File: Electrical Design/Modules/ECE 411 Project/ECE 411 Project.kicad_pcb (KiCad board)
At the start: 2 copper layers, 99.2 x 99.2 mm, 129 parts, among them J1 5mm 9V Barrel, J2 BOOST, J3 Pheonix Connector, J4 1/8in Jack, J5 1/4in Jack, Q2 2N3904, Q3 2N3904, Q4 2N3904, Q5 PNP, Q6 PNP, SW1 SW_Push, SW2 SW_Push, SW3 SW_Push, SW4 SW_Push, SW5 SW_Push, SW6 SW_Push, SW7 SW_Push, SW8 SW_Push, SW9 SW_SPDT, U1 HT7333, U2 LT1054, U3 MN3207, U4 NE555D, U5 LTV-827, U9 TPA3136D2PWPR

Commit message: schematic update
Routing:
- net /ESP32-S3-WROOM Dev Board/GENOUT: track 83.6 -> 116.2 mm, vias 2 -> 3
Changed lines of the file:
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@@
+	)
+	(segment
+		(start 77.9625 35.909448)
+		(end 77.9625 36.7125)
+		(width 0.4)
+		(layer "F.Cu")
+		(net 38)
 	)
 	(segment
@@
 		(net 38)
 	)
+	(segment
+		(start 77.9625 36.7125)
+		(end 79 37.75)
+		(width 0.4)
+		(layer "F.Cu")
+		(net 38)
+	)
 	(via
 		(at 59.8 36.3)
+		(size 0.6)
+		(drill 0.3)
+		(layers "F.Cu" "B.Cu")
+		(free yes)
+		(net 38)
+	)
+	(via
+		(at 79 37.75)
 		(size 0.6)
 		(drill 0.3)
@@
 	)
 	(segment
+		(start 86.45 30.3)
+		(end 98.22 30.3)
+		(width 0.4)
+		(layer "B.Cu")
+		(net 38)
+	)
+	(segment
+		(start 79 37.75)
+		(end 86.45 30.3)
+		(width 0.4)
+		(layer "B.Cu")
+		(net 38)
+	)
+	(segment
 		(start 41.3 41.9)
 		(end 54.2 41.9)
@@
 		(layer "B.Cu")
 		(net 38)
+	)
+	(segment
+		(start 98.22 30.3)
+		(end 103.92 36)
+		(width 0.4)
+		(layer "B.Cu")
+		(net 38)

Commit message: pcb amp revision
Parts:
- removed C2: 4.7uF, Capacitor_SMD:C_1206_3216Metric_Pad1.33x1.80mm_HandSolder
- removed C20: 6.8nF, Capacitor_SMD:C_0805_2012Metric_Pad1.18x1.45mm_HandSolder
- removed C21, C23: 1uF, Capacitor_SMD:C_0805_2012Metric_Pad1.18x1.45mm_HandSolder
- removed CHO-TRE1, OUT_{LINE}1: TestPoint, TestPoint:TestPoint_THTPad_2.5x2.5mm_Drill1.2mm
- removed D3: LED, LED_THT:LED_D5.0mm
- removed R1, R2: 1.2k, Resistor_SMD:R_0805_2012Metric_Pad1.20x1.40mm_HandSolder
- removed R34: 47k, Resistor_SMD:R_0805_2012Metric_Pad1.20x1.40mm_HandSolder
- removed R35: 10k, Resistor_SMD:R_0805_2012Metric_Pad1.20x1.40mm_HandSolder
- removed R36: 470, Resistor_SMD:R_0805_2012Metric_Pad1.20x1.40mm_HandSolder
- removed R37: 100k, Resistor_SMD:R_0805_2012Metric_Pad1.20x1.40mm_HandSolder
- removed R39: 1k, Resistor_SMD:R_0805_2012Metric_Pad1.20x1.40mm_HandSolder
- removed RV1, RV2, RV3, RV7: 10k, Connector_PinSocket_2.54mm:PinSocket_1x03_P2.54mm_Vertical
- removed RV4: 100k Pot, Connector_PinHeader_2.54mm:PinHeader_1x03_P2.54mm_Vertical
- removed RV5: 1k, Connector_PinHeader_2.54mm:PinHeader_1x03_P2.54mm_Vertical
- removed RV6: 100k, Connector_PinSocket_2.54mm:PinSocket_1x03_P2.54mm_Vertical
- removed U4: NE555D, Package_SO:SOIC-8_3.9x4.9mm_P1.27mm
- removed U5: LTV-827, Package_DIP:DIP-8_W7.62mm
- removed V3207D2: ~, Package_DIP:CERDIP-8_W7.62mm_SideBrazed
- added G***: LOGO, LOGO, F.Cu at (103.1, 117.1)
- added M4: MountingHole_4.3mm_M4_Pad_TopBottom, MountingHole:MountingHole_4.3mm_M4_Pad_TopBottom, F.Cu at (38.4, 117.5)
- added REF**: MountingHole_4.3mm_M4_Pad_TopBottom, MountingHole:MountingHole_4.3mm_M4_Pad_TopBottom, F.Cu at (125.1, 118.6)
- C33: value .1uF -> 0.1uF
- J5: value 1/4in Jack -> 01x02 pin header
- L1, L2: footprint Inductor-VLS6045AF_330M:IND_VLS6045AF-330M -> Inductor_THT:RL110-330K-RC
- moved GND1 91.6 mm to (125.1, 96.6)
- moved C28 17.3 mm to (69.0, 101.0)
- moved R40 14.1 mm to (79.0, 109.0), turned to -90 degrees
- moved C29 13.7 mm to (72.2, 95.2), turned to -90 degrees
- moved J5 12.2 mm to (77.9, 97.7), turned to 90 degrees
- moved ? 11.9 mm to (117.8, 113.8)
- moved C26 10.9 mm to (69.7, 95.2), turned to -90 degrees
- moved C24 9.73 mm to (65.9, 96.7), turned to 180 degrees
- moved C37 8.76 mm to (54.0, 96.2)
- moved C33 8.76 mm to (80.0, 103.8), turned to 0 degrees
- moved C32 8.30 mm to (80.0, 106.0)
- moved C27 8.03 mm to (72.0, 116.1)
- moved R43 7.88 mm to (76.0, 101.0)
- moved C35 7.81 mm to (64.9, 104.7), turned to 0 degrees
- moved U9 7.75 mm to (72.2, 107.6)
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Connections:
- SW8 pad 2: /ESP32-S3-WROOM Dev Board/BTN7 -> /BTN7
- U6 pad 13: /ESP32-S3-WROOM Dev Board/SCL -> unconnected-(U6-IO12-Pad13)
- U6 pad 15: /ESP32-S3-WROOM Dev Board/SDA -> GND
- U6 pad 23: /ESP32-S3-WROOM Dev Board/BTN7 -> unconnected-(U6-IO15-Pad23)
- U6 pad 24: /ESP32-S3-WROOM Dev Board/CLK -> unconnected-(U6-IO2-Pad24)
- U6 pad 25: unconnected-(U6-IO0-Pad25) -> /ESP32-S3-WROOM Dev Board/BTN6
- U6 pad 26: unconnected-(U6-IO4-Pad26) -> /ESP32-S3-WROOM Dev Board/BTN5
- U6 pad 27: /ESP32-S3-WROOM Dev Board/BTN6 -> /ESP32-S3-WROOM Dev Board/BTN4
- U6 pad 28: /ESP32-S3-WROOM Dev Board/BTN5 -> /ESP32-S3-WROOM Dev Board/BTN3
- U6 pad 29: /ESP32-S3-WROOM Dev Board/BTN4 -> /ESP32-S3-WROOM Dev Board/BTN2
- U6 pad 30: /ESP32-S3-WROOM Dev Board/BTN3 -> /ESP32-S3-WROOM Dev Board/BTN1
- U6 pad 31: /ESP32-S3-WROOM Dev Board/BTN2 -> /ESP32-S3-WROOM Dev Board/BTN0
- U6 pad 33: /ESP32-S3-WROOM Dev Board/BTN1 -> /ESP32-S3-WROOM Dev Board/SDA
- U6 pad 35: /ESP32-S3-WROOM Dev Board/BTN0 -> unconnected-(U6-TXD0/IO1-Pad35)
- U6 pad 36: unconnected-(U6-IO22-Pad36) -> /ESP32-S3-WROOM Dev Board/SCL
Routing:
- net /Tremolo Effect/TREMOUT: track 102.9 -> 0.00 mm, vias 1 -> 0
- net +9V: track 232.4 -> 162.8 mm
- net /Chorus Effect/CHORUSIN: track 80.7 -> 19.2 mm
- net /Chorus Effect/CHORUSOUT: track 51.5 -> 0.00 mm, vias 2 -> 0
- net Net-(V3207D2-+): track 59.3 -> 16.2 mm, vias 2 -> 0
- net Vin: track 130.9 -> 171.0 mm, vias 8 -> 4
- net /ESP32-S3-WROOM Dev Board/BTN7: track 36.5 -> 0.00 mm
- net (no net): track 0.00 -> 36.5 mm
- net /ESP32-S3-WROOM Dev Board/GENOUT: track 116.2 -> 85.8 mm
- net Net-(U4-THR): track 21.7 -> 0.00 mm, vias 2 -> 0
- net /LineOut: track 17.8 -> 4.15 mm
- net Net-(U4-DIS): track 12.4 -> 0.00 mm
- net +4.5V: track 104.1 -> 92.2 mm
- net /Class-D Amplification/SPK+: track 30.5 -> 42.1 mm
- net Net-(Q6-E): track 22.8 -> 11.9 mm
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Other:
- board size 99.2 x 99.2 mm -> 99.2 x 97.1 mm
- board text added: "1/4{dblquote} OUT"
- board text added: "LINE OUT"

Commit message: pcb redo b2.1
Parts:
- removed CLK1: TestPoint, TestPoint:TestPoint_THTPad_2.5x2.5mm_Drill1.2mm
- removed SW8: SW_Push, Connector_PinHeader_2.54mm:PinHeader_1x02_P2.54mm_Vertical
- added C2: 4.7uF, Capacitor_SMD:C_1206_3216Metric_Pad1.33x1.80mm_HandSolder, F.Cu at (151.5, 126.8)
- added C20: 6.8nF, Capacitor_SMD:C_0805_2012Metric_Pad1.18x1.45mm_HandSolder, F.Cu at (190.1, 89.8)
- added C21: 1uF, Capacitor_SMD:C_0805_2012Metric_Pad1.18x1.45mm_HandSolder, F.Cu at (190.1, 92.8)
- added C23: 1uF, Capacitor_SMD:C_0805_2012Metric_Pad1.18x1.45mm_HandSolder, F.Cu at (161.5, 106.3)
- added CHO-TRE1: TestPoint, TestPoint:TestPoint_THTPad_2.5x2.5mm_Drill1.2mm, F.Cu at (110.7, 37.0)
- added D3: LED, LED_THT:LED_D5.0mm, F.Cu at (151.0, 121.4)
- added J6: 1x2header, Connector_PinSocket_2.54mm:PinSocket_1x02_P2.54mm_Vertical, F.Cu at (139.0, 100.0)
- added J7: 1x2header, Connector_PinSocket_2.54mm:PinSocket_1x02_P2.54mm_Vertical, F.Cu at (92.8, 42.3)
- added OUT_{LINE}1: TestPoint, TestPoint:TestPoint_THTPad_2.5x2.5mm_Drill1.2mm, F.Cu at (151.4, 111.7)
- added R1: 1.2k, Resistor_SMD:R_0805_2012Metric_Pad1.20x1.40mm_HandSolder, F.Cu at (153.1, 130.8)
- added R2: 1.2k, Resistor_SMD:R_0805_2012Metric_Pad1.20x1.40mm_HandSolder, F.Cu at (153.1, 133.8)
- added R34: 47k, Resistor_SMD:R_0805_2012Metric_Pad1.20x1.40mm_HandSolder, F.Cu at (190.1, 78.0)
- added R35: 10k, Resistor_SMD:R_0805_2012Metric_Pad1.20x1.40mm_HandSolder, F.Cu at (190.1, 80.9)
- added R36: 470, Resistor_SMD:R_0805_2012Metric_Pad1.20x1.40mm_HandSolder, F.Cu at (190.1, 83.8)
- added R37: 100k, Resistor_SMD:R_0805_2012Metric_Pad1.20x1.40mm_HandSolder, F.Cu at (190.1, 86.8)
- added R39: 1k, Resistor_SMD:R_0805_2012Metric_Pad1.20x1.40mm_HandSolder, F.Cu at (156.1, 109.8)
- added R9: 4.7k, Resistor_SMD:R_0805_2012Metric_Pad1.20x1.40mm_HandSolder, F.Cu at (78.9, 32.7)
- added REF**: MountingHole_4.3mm_M4_Pad_TopBottom, MountingHole:MountingHole_4.3mm_M4_Pad_TopBottom, F.Cu at (126.6, 28.7)
- added REF**: MountingHole_4.3mm_M4_Pad_TopBottom, MountingHole:MountingHole_4.3mm_M4_Pad_TopBottom, F.Cu at (36.7, 28.7)
- added RV1: 10k, Connector_PinSocket_2.54mm:PinSocket_1x02_P2.54mm_Vertical, F.Cu at (94.9, 29.4)
- added RV2: 10k, Connector_PinSocket_2.54mm:PinSocket_1x02_P2.54mm_Vertical, F.Cu at (110.7, 29.3)
- added RV3: 10k, Connector_PinSocket_2.54mm:PinSocket_1x02_P2.54mm_Vertical, F.Cu at (157.4, 100.0)
- added RV4: 100k Pot, Connector_PinHeader_2.54mm:PinHeader_1x03_P2.54mm_Vertical, F.Cu at (90.8, 29.3)
- added RV5: 1k, Connector_PinSocket_2.54mm:PinSocket_1x03_P2.54mm_Vertical, F.Cu at (86.5, 29.3)
- added RV6: 100k, Connector_PinSocket_2.54mm:PinSocket_1x02_P2.54mm_Vertical, F.Cu at (140.0, 131.7)
- added RV7: 10k, Connector_PinSocket_2.54mm:PinSocket_1x02_P2.54mm_Vertical, F.Cu at (80.3, 92.2)
- added RV8: 100k, Connector_PinSocket_2.54mm:PinSocket_1x03_P2.54mm_Vertical, F.Cu at (77.3, 29.2)
- added SW10: SW_SPDT, Button_Switch_THT:SW_Slide_SPDT_Angled_CK_OS102011MA1Q, F.Cu at (104.8, 26.9)
- added TP1: Line In, TestPoint:TestPoint_Bridge_Pitch2.0mm_Drill0.7mm, F.Cu at (155.4, 106.5)
- added U4: NE555D, Package_SO:SOIC-8_3.9x4.9mm_P1.27mm, F.Cu at (146.5, 132.7)
- added U5: LTV-827, Package_DIP:DIP-8_W7.62mm, F.Cu at (139.3, 119.7)
- added V3207D2: ~, Package_DIP:CERDIP-8_W7.62mm_SideBrazed, F.Cu at (178.5, 80.0)
- J5: value 01x02 pin header -> 1x2 header
- moved V4.5 96.6 mm to (149.4, 142.3)
- moved C18 80.5 mm to (173.1, 67.2)
- moved C19 80.5 mm to (173.1, 70.2), turned to 0 degrees
- moved C17 74.3 mm to (173.1, 64.1)
- moved R32 63.8 mm to (152.2, 81.8), turned to 0 degrees
- moved C15 61.9 mm to (168.3, 70.2), turned to 0 degrees
- moved C16 60.1 mm to (168.3, 73.2)
- moved U3 59.3 mm to (156.2, 83.6), turned to 0 degrees
- moved Q4 58.5 mm to (156.6, 77.5), turned to 0 degrees
- moved C41 55.8 mm to (173.1, 73.2), turned to 0 degrees
- moved R3 53.6 mm to (142.7, 64.1), turned to 0 degrees
- moved C13 53.1 mm to (168.3, 64.1), turned to 0 degrees
- moved C14 48.9 mm to (168.3, 67.2)
- moved Q3 48.2 mm to (156.6, 71.7), turned to 0 degrees
- moved R31 48.1 mm to (152.2, 78.9), turned to 0 degrees
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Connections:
- net /ESP32-S3-WROOM Dev Board/SCL renamed /SCL
- net /ESP32-S3-WROOM Dev Board/SDA renamed /SDA
- C38 pad 1: /ESP32-S3-WROOM Dev Board/GENOUT -> /FX
- FUZ-CHO1 pad 1: /Chorus Effect/CHORUSIN -> /Fuzz Schematic/FUZZOUT
- Q2 pad 3: +9V -> /Chorus Effect/Vin
- Q3 pad 3: +9V -> /Chorus Effect/Vin
- Q4 pad 3: +9V -> /Chorus Effect/Vin
- R16 pad 2: +4.5V -> /Chorus Effect/V.5in
- R20 pad 1: +4.5V -> /Chorus Effect/V.5in
- R28 pad 2: +4.5V -> /Chorus Effect/V.5in
- SW3 pad 2: /ESP32-S3-WROOM Dev Board/BTN2 -> /ESP32-S3-WROOM Dev Board/BTN1
- SW9 pad 1: /ESP32-S3-WROOM Dev Board/GENOUT -> /FX
- SW9 pad 3: /Tremolo Effect/TREMOUT -> /Amp
- U6 pad 1: unconnected-(U6-3V3-Pad1) -> /ESP32-S3-WROOM Dev Board/MCU3v3
- U6 pad 10: unconnected-(U6-IO26-Pad10) -> /ESP32-S3-WROOM Dev Board/BTN3
- U6 pad 11: unconnected-(U6-IO27-Pad11) -> /ESP32-S3-WROOM Dev Board/BTN1
- U6 pad 12: unconnected-(U6-IO14-Pad12) -> /ESP32-S3-WROOM Dev Board/BTN1
- U6 pad 13: unconnected-(U6-IO12-Pad13) -> /ESP32-S3-WROOM Dev Board/BTN0
- U6 pad 25: /ESP32-S3-WROOM Dev Board/BTN6 -> unconnected-(U6-IO0-Pad25)
- U6 pad 26: /ESP32-S3-WROOM Dev Board/BTN5 -> unconnected-(U6-IO4-Pad26)
- U6 pad 27: /ESP32-S3-WROOM Dev Board/BTN4 -> unconnected-(U6-IO16-Pad27)
- U6 pad 28: /ESP32-S3-WROOM Dev Board/BTN3 -> unconnected-(U6-IO17-Pad28)
- U6 pad 29: /ESP32-S3-WROOM Dev Board/BTN2 -> unconnected-(U6-IO5-Pad29)
- U6 pad 30: /ESP32-S3-WROOM Dev Board/BTN1 -> unconnected-(U6-IO18-Pad30)
- U6 pad 31: /ESP32-S3-WROOM Dev Board/BTN0 -> unconnected-(U6-IO19-Pad31)
- U6 pad 5: unconnected-(U6-IO34-Pad5) -> /ESP32-S3-WROOM Dev Board/FREQ
- U6 pad 6: unconnected-(U6-IO35-Pad6) -> /FX
- U6 pad 7: unconnected-(U6-IO32-Pad7) -> /ESP32-S3-WROOM Dev Board/BTN6
- U6 pad 8: unconnected-(U6-IO33-Pad8) -> /ESP32-S3-WROOM Dev Board/BTN5
- U6 pad 9: /ESP32-S3-WROOM Dev Board/GENOUT -> /ESP32-S3-WROOM Dev Board/BTN4
- V3207D1 pad 3: +9V -> /Chorus Effect/Vin
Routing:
- net /FX: track 0.00 -> 94.5 mm
- net +4.5V: track 92.2 -> 2.00 mm, vias 6 -> 0
- net /ESP32-S3-WROOM Dev Board/GENOUT: track 85.8 -> 0.00 mm, vias 3 -> 0
- net Net-(U3-IN): track 53.0 -> 0.00 mm
- net +9V: track 162.8 -> 111.6 mm, vias 5 -> 3
- net /SDA: track 54.8 -> 5.15 mm
- net /Amp: track 0.00 -> 47.3 mm, vias 0 -> 2
- net /SCL: track 52.3 -> 5.25 mm
- net (no net): track 36.5 -> 0.00 mm
- net Net-(C12-Pad1): track 34.8 -> 0.00 mm
- net Net-(Q6-E): track 11.9 -> 36.8 mm
- net Net-(U3-OUT1): track 22.2 -> 0.00 mm
- net Net-(Q4-E): track 20.8 -> 0.00 mm
- net /Fuzz Schematic/FUZZOUT: track 0.00 -> 19.6 mm
- net +5V: track 118.3 -> 99.6 mm
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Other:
- board size 99.2 x 97.1 mm -> 99.8 x 99.9 mm
- board text added: "Vol"
- board text added: "r1.4 | 17 November 2024"
- board text removed: "r1.1 14 November 2024"

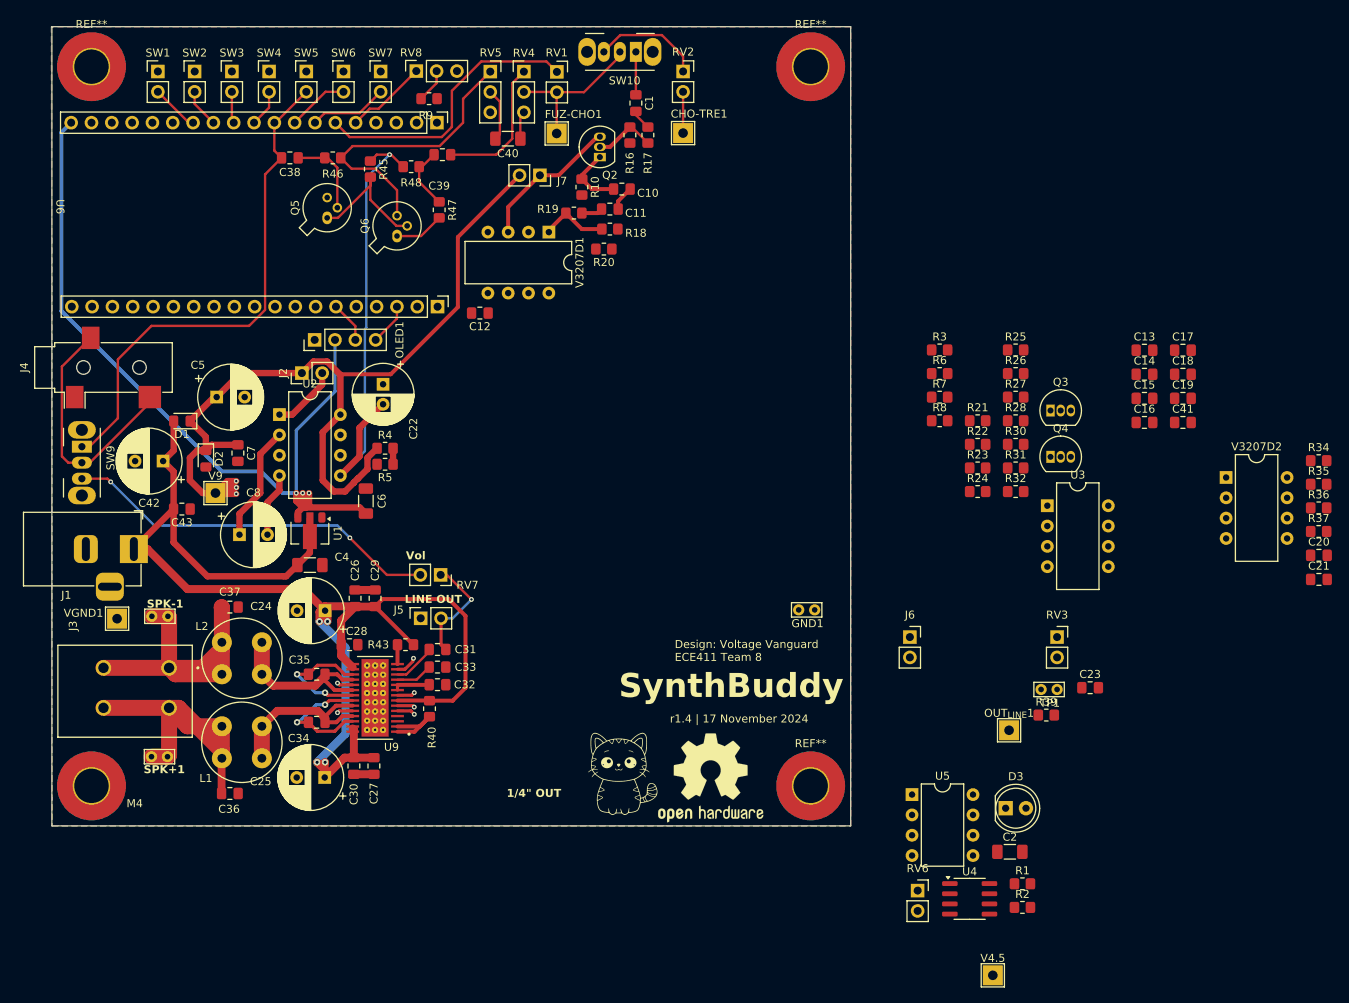
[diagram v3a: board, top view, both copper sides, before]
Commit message: new space-optimized PCB layout
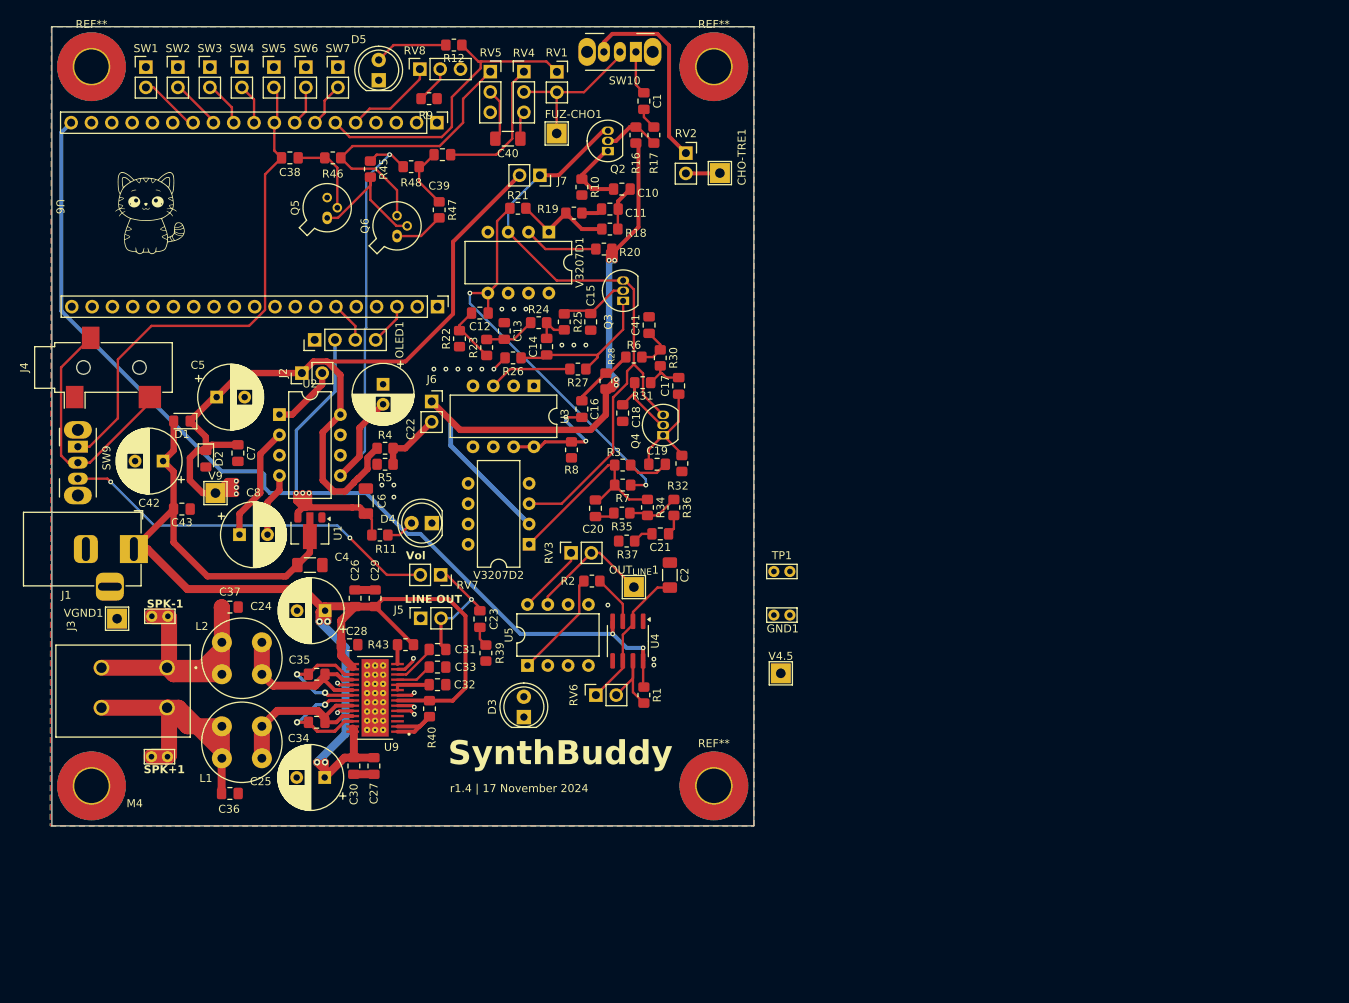
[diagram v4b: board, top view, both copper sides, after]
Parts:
- removed ?: , clipboard:cb89ceac-0acd-432b-9393-97274f22b4f5
- added D4: LED, LED_THT:LED_D5.0mm, F.Cu at (79.2, 85.8)
- added D5: LED, LED_THT:LED_D5.0mm, F.Cu at (72.6, 30.4)
- added R11: 1.2k, Resistor_SMD:R_0805_2012Metric_Pad1.20x1.40mm_HandSolder, F.Cu at (72.8, 87.2)
- added R12: 1.2k, Resistor_SMD:R_0805_2012Metric_Pad1.20x1.40mm_HandSolder, F.Cu at (82.0, 26.0)
- moved G*** 91.7 mm to (44.0, 47.0)
- moved C20 90.6 mm to (99.7, 83.9), turned to -90 degrees
- moved V3207D2 87.5 mm to (91.4, 88.4), turned to 180 degrees
- moved R35 87.2 mm to (103.0, 84.5)
- moved R37 86.5 mm to (103.6, 88.0)
- moved R34 84.1 mm to (106.2, 83.8), turned to -90 degrees
- moved C21 82.5 mm to (107.8, 87.1), turned to 180 degrees
- moved R36 80.6 mm to (109.5, 83.8), turned to -90 degrees
- moved C13 80.1 mm to (88.3, 61.7), turned to -90 degrees
- moved C23 76.8 mm to (85.2, 97.8), turned to -90 degrees
- moved C14 74.8 mm to (93.6, 63.7), turned to 90 degrees
- moved R39 70.5 mm to (86.0, 102.0), turned to 90 degrees
- moved C16 70.3 mm to (98.0, 71.5), turned to 90 degrees
- moved C18 70.2 mm to (103.1, 72.0), turned to 90 degrees
- moved C15 69.9 mm to (99.1, 60.6), turned to 90 degrees
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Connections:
- R1 pad 1: +9V -> +5V
- U4 pad 4: +9V -> +5V
- U4 pad 8: +9V -> +5V
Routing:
- net /Chorus Effect/V.5in: track 0.00 -> 85.8 mm, vias 0 -> 4
- net /Chorus Effect/Vin: track 18.2 -> 80.7 mm
- net +5V: track 99.6 -> 161.6 mm, vias 3 -> 5
- net Net-(C12-Pad1): track 0.00 -> 51.5 mm, vias 0 -> 2
- net Net-(V3207D2-+): track 0.00 -> 25.3 mm
- net Net-(Q3-E): track 0.00 -> 20.2 mm
- net Net-(U4-THR): track 0.00 -> 18.2 mm
- net /Amp: track 47.3 -> 63.6 mm
- net Net-(U3-OUT1): track 0.00 -> 15.4 mm, vias 0 -> 2
- net Net-(Q4-E): track 0.00 -> 13.9 mm
- net Net-(R2-Pad2): track 0.00 -> 13.5 mm
- net Net-(U4-DIS): track 0.00 -> 11.0 mm
- net Net-(SW10-C): track 13.8 -> 24.7 mm
- net Net-(U3-IN): track 0.00 -> 10.4 mm
- net /Chorus Effect/CHORUSOUT: track 5.16 -> 15.5 mm
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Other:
- board size 99.8 x 99.9 mm -> 87.8 x 99.9 mm
- board text removed: "1/4{dblquote} OUT"
- board text removed: "Design: Voltage Vanguard ECE411 Team 8"
